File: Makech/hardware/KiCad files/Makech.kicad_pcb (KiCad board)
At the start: 2 copper layers, 54.9 x 88.5 mm, 54 parts, among them IC1 ULN2803, J1 SWD programmer, J2 USB_B_Micro, J3 ESP32-Exp, J4 Conn_02x05_Odd_Even, SW1 RST, SW2 SW_DPDT_x2, U1 ATSAMD21G18A-AU, U2 CONN_01X04, U3 AP2114_3.3v, X1 Screw_Terminal_1x02

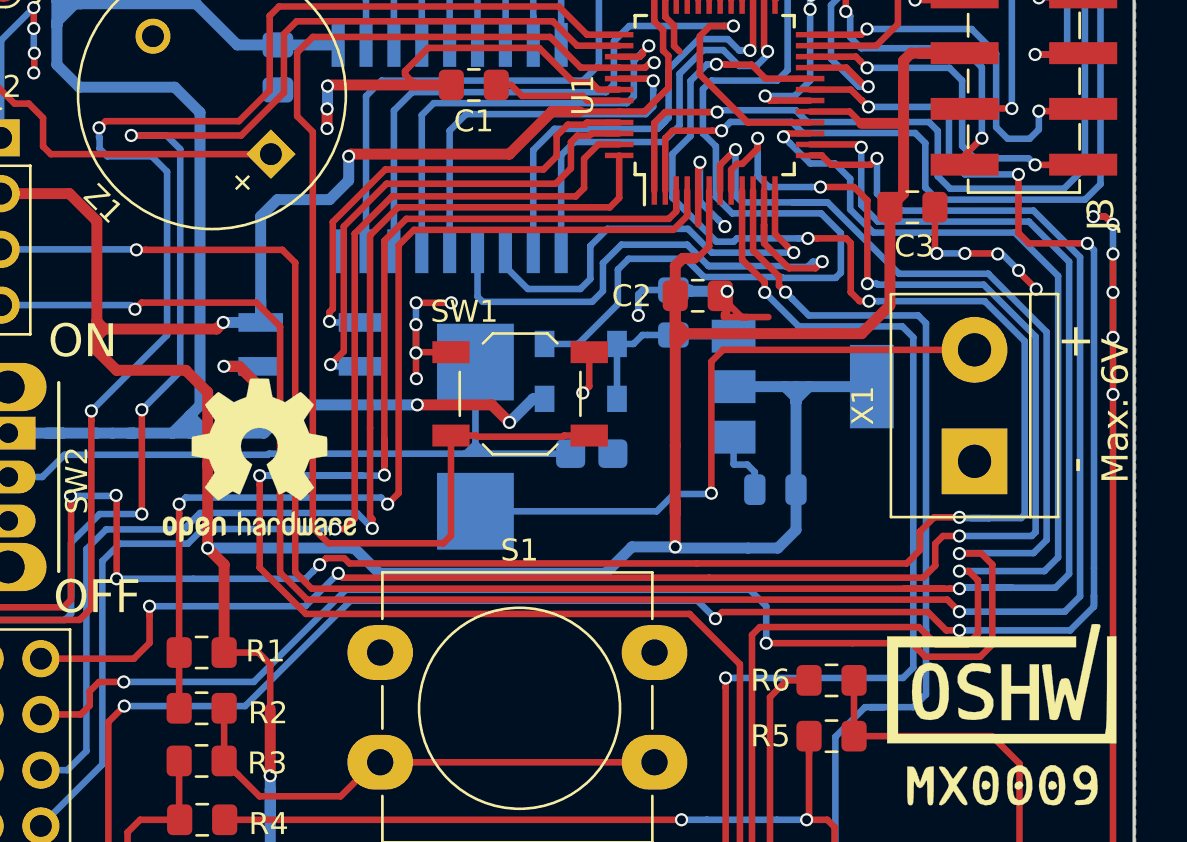
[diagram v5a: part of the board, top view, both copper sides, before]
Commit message: Update vias
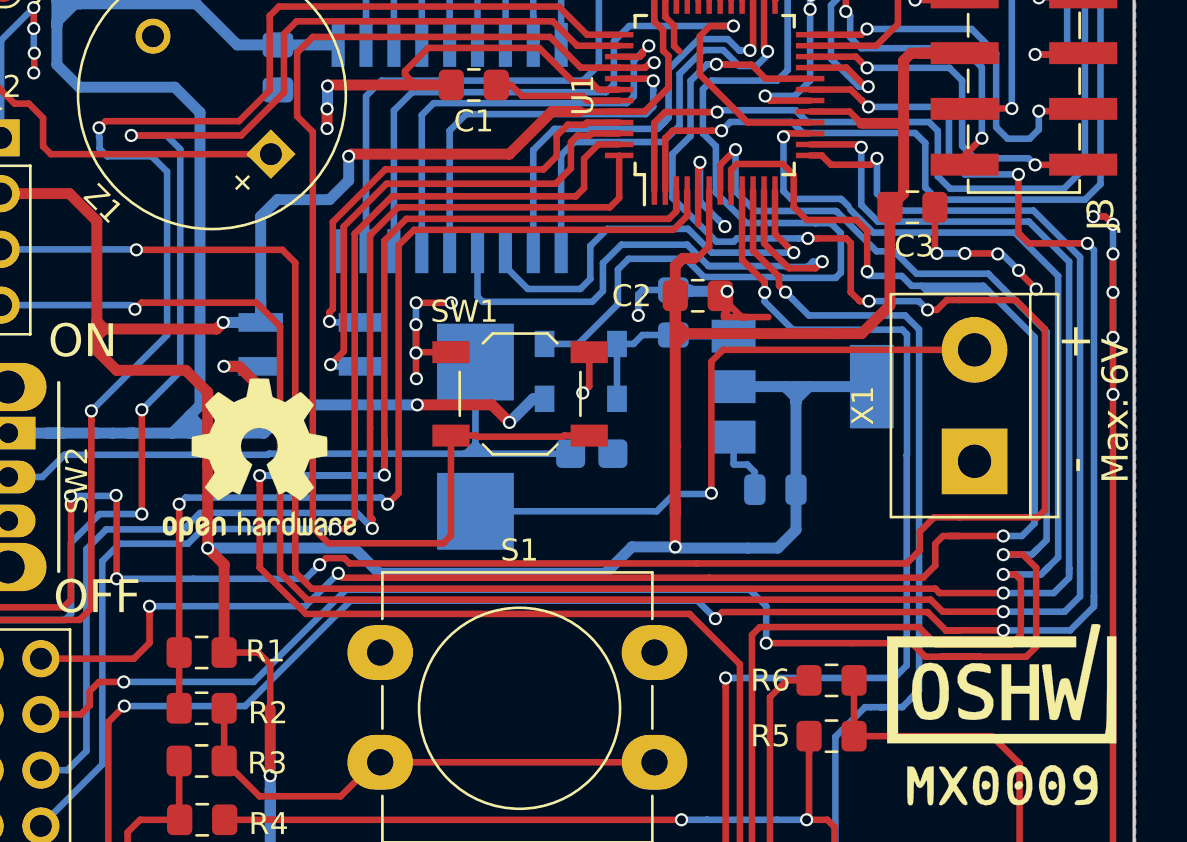
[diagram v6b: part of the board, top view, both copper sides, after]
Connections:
- net /ESP_BUSY renamed /ESP_BUSY_ACK
- net /ESP_CS renamed /ESP_CS_RTS
- net /ESP_GPIO renamed /ESP_GPIO0
- net /ESP_MISO renamed /ESP_MISO_RX
- net /ESP_MOSI renamed /ESP_MOSI_TX
- net /ESP_SCK renamed /ESP_SCK_CTS
- J3 pad 9: /ESP_RTS -> Net-(J3-Pad9)
- U1 pad 28: /ESP_RTS -> Net-(U1-Pad28)
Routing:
- net /D32: track 81.4 -> 90.4 mm, vias 6 -> 4
- net /SCL: track 98.8 -> 94.1 mm
- net /D34: track 109.7 -> 111.3 mm
- net /A3: track 64.7 -> 66.2 mm
- net /A2: track 82.1 -> 81.0 mm
- net /D33: track 104.7 -> 105.3 mm
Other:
- net class source: clearance 0.2 -> 0.45

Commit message: brush traces
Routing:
- net Net-(D1-Pad1): track 33.1 -> 56.9 mm
- net /D32: track 90.4 -> 88.3 mm
- net +6V: track 104.0 -> 105.8 mm
- net /D31: track 90.5 -> 92.0 mm
- net /D35: track 66.1 -> 67.6 mm
- net /A4: track 45.9 -> 47.3 mm
- net /D33: track 105.3 -> 106.6 mm
- net Net-(JP1-Pad2): track 19.5 -> 18.5 mm
- net /D30: track 53.1 -> 54.1 mm
- net /D34: track 111.3 -> 110.6 mm
- net +3V3: track 194.2 -> 193.5 mm
- net /D36: track 58.7 -> 59.4 mm

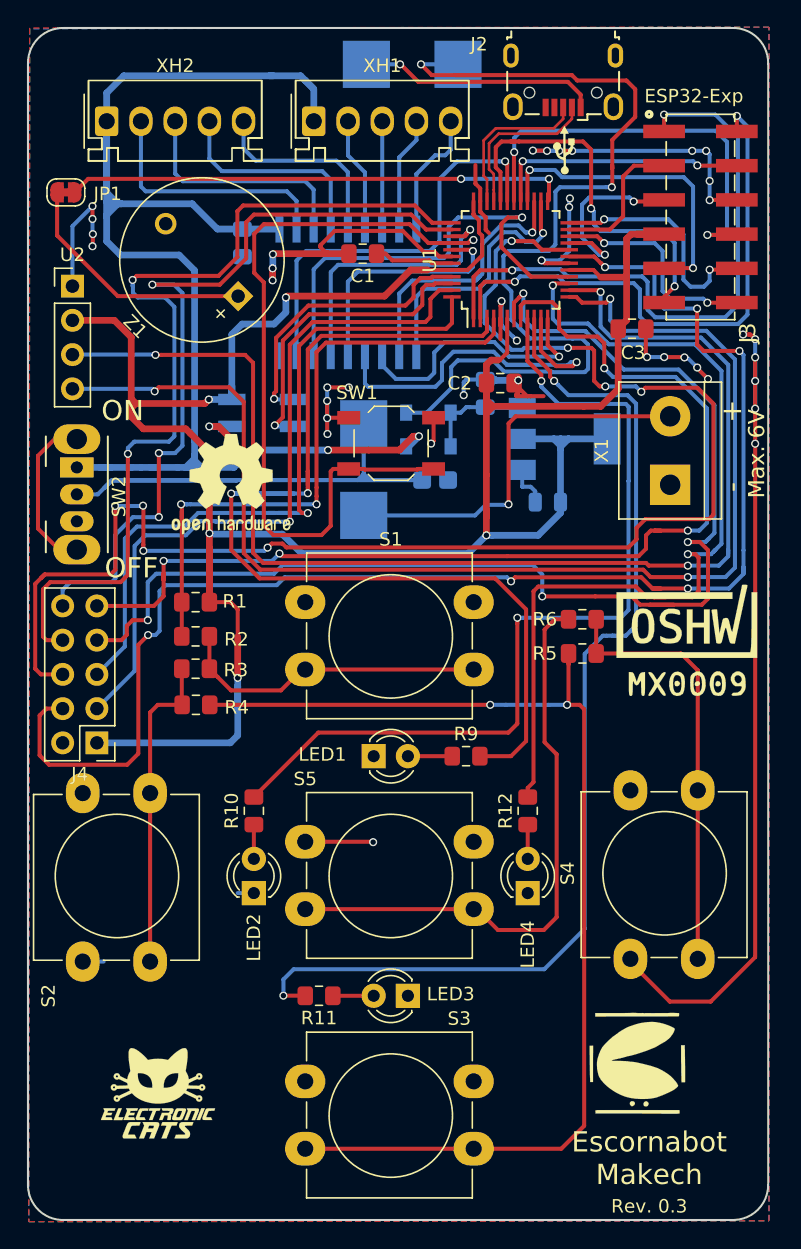
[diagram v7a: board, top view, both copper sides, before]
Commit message: Add footprint to local library erase track
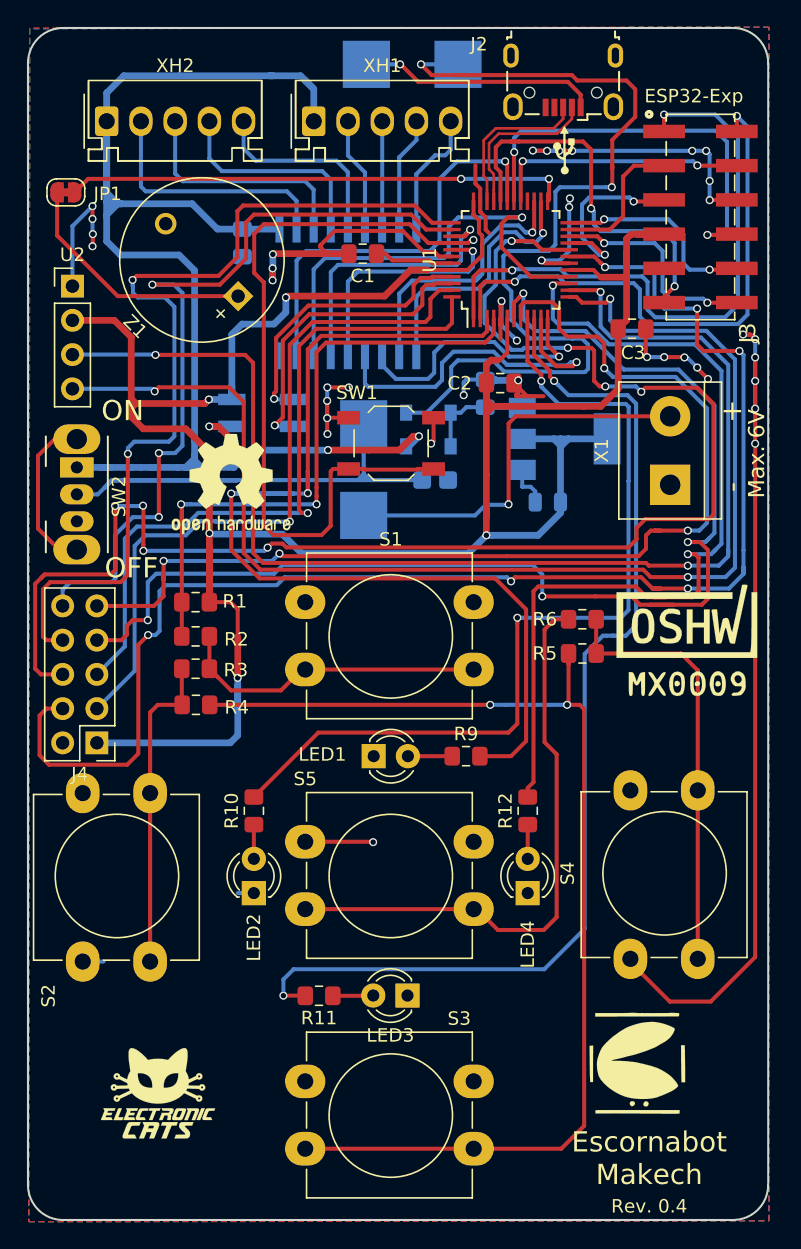
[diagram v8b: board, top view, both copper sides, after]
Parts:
- J3: footprint Pines:610X1221121 -> pines:610X1221121
- LED3: footprint LEDs:LED_D3.0mm -> LED_THT:LED_D3.0mm
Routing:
- net /ESP_RTS: track 23.2 -> 0.00 mm, vias 2 -> 0
- net /ESP_SCK_CTS: track 17.6 -> 15.4 mm
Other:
- board text added: "Rev. 0.4"
- board text removed: "Rev. 0.3"
